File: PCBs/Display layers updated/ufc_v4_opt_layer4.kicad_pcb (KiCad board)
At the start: 2 copper layers, 43.1 x 15.9 mm, 66 parts

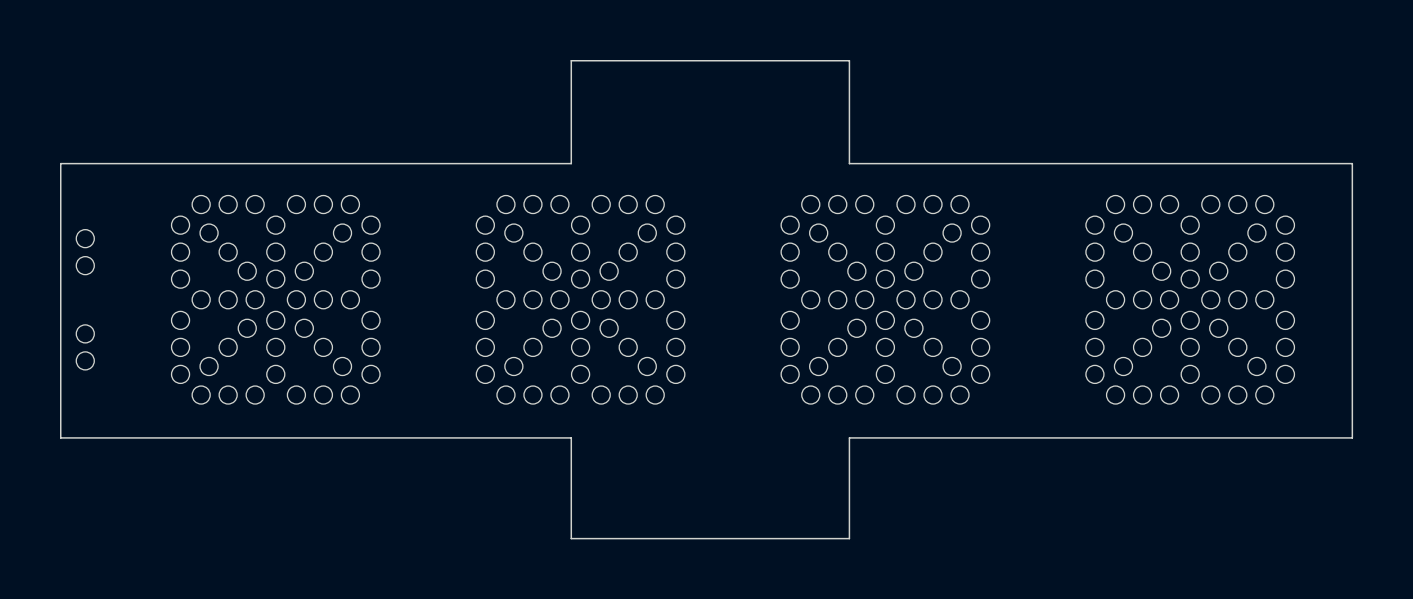
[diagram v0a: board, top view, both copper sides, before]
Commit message: Updated PCBs, cleaned up files
No commit for a while; a lot has happened in the mean time. JLC refused my order for the display layers, so I settled for just the dot layer. The gerbers for the rest are deleted, but the kicad files are still present.

I also received the main PCBs from JLC, and edited a couple small details.
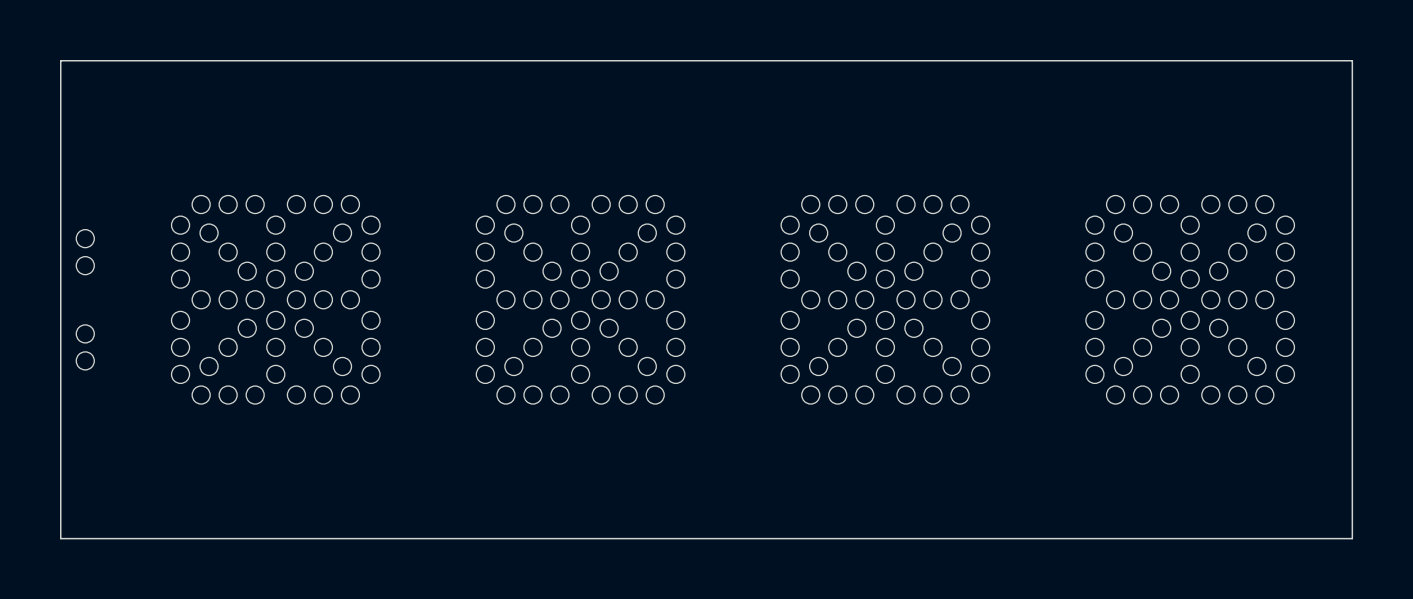
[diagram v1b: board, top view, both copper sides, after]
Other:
- outline, holes or cut-outs redrawn
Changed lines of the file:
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@@
   (general
     (thickness 1.6)
-    (drawings 15)
+    (drawings 7)
     (tracks 0)
     (zones 0)
@@
       (usegerberattributes false)
       (usegerberadvancedattributes false)
-      (creategerberjobfile false)
+      (creategerberjobfile true)
       (excludeedgelayer true)
       (linewidth 0.100000)
@@
       (drillshape 0)
       (scaleselection 1)
-      (outputdirectory "gerber"))
+      (outputdirectory "../Gerbers/Display layers/OPT layer 4/"))
   )
   (net 0 "")
@@
     (effects (font (size 1 1) (thickness 0.15)) (justify mirror))
   )
-  (gr_line (start 121.519 84.072) (end 130.79 84.072) (layer Edge.Cuts) (width 0.05))
-  (gr_line (start 121.519 100.001) (end 130.79 100.001) (layer Edge.Cuts) (width 0.05))
-  (gr_line (start 147.554 87.501) (end 147.554 96.645) (layer Edge.Cuts) (width 0.05))
-  (gr_line (start 104.501 87.501) (end 104.501 96.645) (layer Edge.Cuts) (width 0.05))
-  (gr_line (start 121.519 96.645) (end 104.501 96.645) (layer Edge.Cuts) (width 0.05))
-  (gr_line (start 121.519 100.001) (end 121.519 96.645) (layer Edge.Cuts) (width 0.05))
-  (gr_line (start 130.79 96.645) (end 147.554 96.645) (layer Edge.Cuts) (width 0.05))
-  (gr_line (start 130.79 100.001) (end 130.79 96.645) (layer Edge.Cuts) (width 0.05))
-  (gr_line (start 130.79 87.501) (end 147.554 87.501) (layer Edge.Cuts) (width 0.05))
-  (gr_line (start 130.79 87.501) (end 130.79 84.072) (layer Edge.Cuts) (width 0.05))
-  (gr_line (start 121.519 87.501) (end 121.519 84.072) (layer Edge.Cuts) (width 0.05))
-  (gr_line (start 104.501 87.501) (end 121.519 87.501) (layer Edge.Cuts) (width 0.05))
+  (gr_line (start 104.501 84.072) (end 147.554 84.072) (layer Edge.Cuts) (width 0.05))
+  (gr_line (start 104.501 100.001) (end 147.554 100.001) (layer Edge.Cuts) (width 0.05))
+  (gr_line (start 147.554 84.072) (end 147.554 100.001) (layer Edge.Cuts) (width 0.05))
+  (gr_line (start 104.501 84.072) (end 104.501 100.001) (layer Edge.Cuts) (width 0.05))
   (gr_text "THIS SIDE DOWN" (at 106.9225 92.0275 90) (layer B.SilkS)
     (effects (font (size 0.6 0.6) (thickness 0.15)) (justify mirror))
